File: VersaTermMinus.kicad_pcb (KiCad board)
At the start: 2 copper layers, 86.2 x 78 mm, 61 parts, among them CN1 HDMI_A, CN2 DE15_Socket, CN3 USB_B_Micro, CN5 USB-A, CN6 Mini-DIN-6, CN7 TTL Serial, CN8 DE9 Socket, J2 USBDATA, Q1 2N7002, Q2 2N7002, Q3 2N7002, Q4 2N7002, Q5 2N7002, Q6 2N7002, Q7 2N7002, SW1 RESET, SW2 DEFAULTS, SW3 3V3/5V, U1 Raspberry Pi Pico, U3 MAX3232

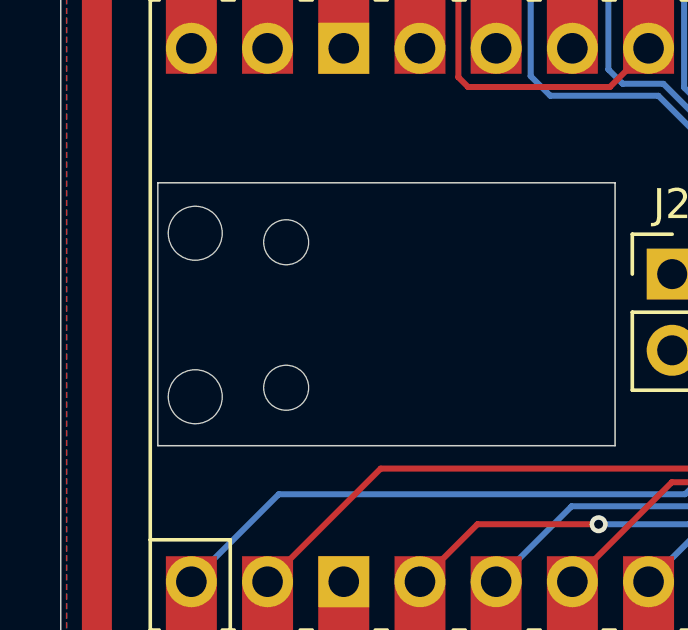
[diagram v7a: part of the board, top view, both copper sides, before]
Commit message: remove ambiguous drill holes
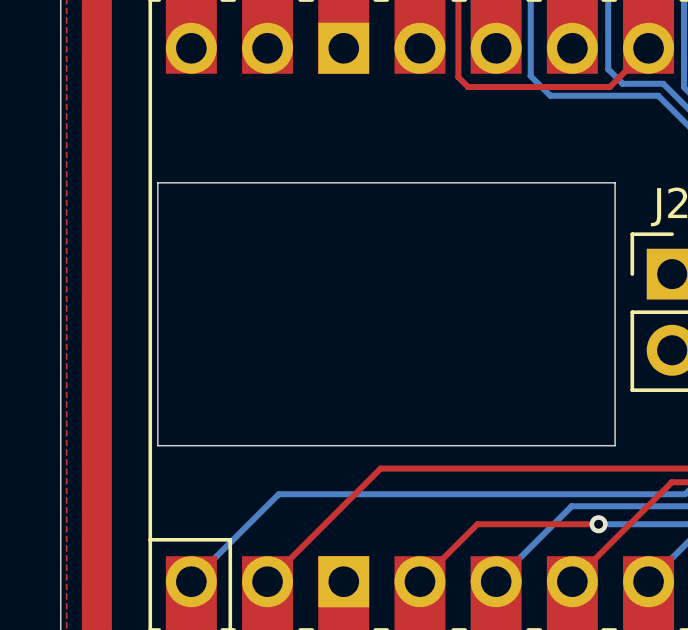
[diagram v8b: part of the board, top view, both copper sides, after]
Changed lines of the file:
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@@
 	(net 81 "RESET")
 	(net 82 "DEFAULTS")
-	(net 83 "unconnected-(U1-GND-Pad42)")
-	(net 84 "unconnected-(U1-3v3_EN-Pad37)")
-	(net 85 "unconnected-(CN6-Pad1)")
-	(net 86 "unconnected-(U1-SWDIO-Pad43)")
-	(net 87 "unconnected-(U1-SWCLK-Pad41)")
-	(net 88 "unconnected-(U1-ADC_VREF-Pad35)")
-	(net 89 "unconnected-(CN6-Pad5)")
-	(net 90 "unconnected-(U1-3v3_EN-Pad37)_1")
-	(net 91 "unconnected-(U1-ADC_VREF-Pad35)_1")
-	(net 92 "unconnected-(U1-VBUS-Pad40)")
-	(net 93 "unconnected-(U1-SWDIO-Pad43)_1")
-	(net 94 "unconnected-(U1-SWCLK-Pad41)_1")
-	(net 95 "unconnected-(U1-VBUS-Pad40)_1")
-	(net 96 "unconnected-(U1-GND-Pad42)_1")
-	(net 97 "/Sync")
-	(net 98 "/Red")
-	(net 99 "/Green")
-	(net 100 "/Blue")
+	(net 83 "unconnected-(CN6-Pad1)")
+	(net 84 "unconnected-(U1-ADC_VREF-Pad35)")
+	(net 85 "unconnected-(CN6-Pad5)")
+	(net 86 "unconnected-(U1-3v3_EN-Pad37)_1")
+	(net 87 "unconnected-(U1-VBUS-Pad40)")
+	(net 88 "unconnected-(U1-SWDIO-Pad43)_1")
+	(net 89 "unconnected-(U1-SWCLK-Pad41)_1")
+	(net 90 "unconnected-(U1-GND-Pad42)_1")
+	(net 91 "/Sync")
+	(net 92 "/Red")
+	(net 93 "/Green")
+	(net 94 "/Blue")
 	(footprint "Resistor_SMD:R_0805_2012Metric_Pad1.20x1.40mm_HandSolder"
 		(layer "F.Cu")
@@
 			(layers "F.Cu" "F.Paste" "F.Mask")
 			(roundrect_rratio 0.208333)
-			(net 98 "/Red")
+			(net 92 "/Red")
 			(pintype "passive")
 		)
@@
 			(layers "*.Cu" "*.Mask")
 			(remove_unused_layers no)
-			(net 85 "unconnected-(CN6-Pad1)")
+			(net 83 "unconnected-(CN6-Pad1)")
 			(pintype "passive+no_connect")
 		)
@@
 			(layers "*.Cu" "*.Mask")
 			(remove_unused_layers no)
-			(net 89 "unconnected-(CN6-Pad5)")
+			(net 85 "unconnected-(CN6-Pad5)")
 			(pintype "passive+no_connect")
 		)
@@
 			(layers "F.Cu" "F.Paste" "F.Mask")
 			(roundrect_rratio 0.208333)
-			(net 100 "/Blue")
+			(net 94 "/Blue")
 			(pintype "passive")
 		)
@@
 			(layer "F.SilkS")
 		)
-		(fp_poly
-			(pts
-				(xy 3.7 -20.2) (xy -3.7 -20.2) (xy -3.7 -24.9) (xy 3.7 -24.9)
-			)
-			(stroke
-				(width 0.1)
-				(type solid)
-			)
-			(fill solid)
-			(layer "Dwgs.User")
-		)
-		(fp_poly
-			(pts
-				(xy -1.5 -16.5) (xy -3.5 -16.5) (xy -3.5 -18.5) (xy -1.5 -18.5)
-			)
-			(stroke
-				(width 0.1)
-				(type solid)
-			)
-			(fill solid)
-			(layer "Dwgs.User")
-		)
-		(fp_poly
-			(pts
-				(xy -1.5 -14) (xy -3.5 -14) (xy -3.5 -16) (xy -1.5 -16)
-			)
-			(stroke
-				(width 0.1)
-				(type solid)
-			)
-			(fill solid)
-			(layer "Dwgs.User")
-		)
-		(fp_poly
-			(pts
-				(xy -1.5 -11.5) (xy -3.5 -11.5) (xy -3.5 -13.5) (xy -1.5 -13.5)
-			)
-			(stroke
-				(width 0.1)
-				(type solid)
-			)
-			(fill solid)
-			(layer "Dwgs.User")
-		)
 		(fp_line
 			(start 11 -26)
@@
 			)
 		)
-		(pad "" np_thru_hole oval
-			(at -2.725 -24 90)
-			(size 1.8 1.8)
-			(drill 1.8)
-			(layers "*.Cu" "*.Mask")
-		)
-		(pad "" np_thru_hole oval
-			(at -2.425 -20.97 90)
-			(size 1.5 1.5)
-			(drill 1.5)
-			(layers "*.Cu" "*.Mask")
-		)
-		(pad "" np_thru_hole oval
-			(at 2.425 -20.97 90)
-			(size 1.5 1.5)
-			(drill 1.5)
-			(layers "*.Cu" "*.Mask")
-		)
-		(pad "" np_thru_hole oval
-			(at 2.725 -24 90)
-			(size 1.8 1.8)
-			(drill 1.8)
-			(layers "*.Cu" "*.Mask")
-		)
 		(pad "1" thru_hole oval
 			(at -8.89 -24.13 90)
@@
 			(layers "*.Cu" "*.Mask")
 			(remove_unused_layers no)
-			(net 88 "unconnected-(U1-ADC_VREF-Pad35)")
+			(net 84 "unconnected-(U1-ADC_VREF-Pad35)")
 			(pinfunction "ADC_VREF")
 			(pintype "input+no_connect")
@@
 			)
 			(layers "F.Cu" "F.Mask")
-			(net 91 "unconnected-(U1-ADC_VREF-Pad35)_1")
+			(net 84 "unconnected-(U1-ADC_VREF-Pad35)")
 			(pinfunction "ADC_VREF")
 			(pintype "input+no_connect")
@@
 			(layers "*.Cu" "*.Mask")
 			(remove_unused_layers no)
-			(net 90 "unconnected-(U1-3v3_EN-Pad37)_1")
+			(net 86 "unconnected-(U1-3v3_EN-Pad37)_1")
 			(pinfunction "3v3_EN")
 			(pintype "input+no_connect")
@@
 			)
 			(layers "F.Cu" "F.Mask")
-			(net 84 "unconnected-(U1-3v3_EN-Pad37)")
+			(net 86 "unconnected-(U1-3v3_EN-Pad37)_1")
 			(pinfunction "3v3_EN")
 			(pintype "input+no_connect")
@@
 			(layers "*.Cu" "*.Mask")
 			(remove_unused_layers no)
-			(net 92 "unconnected-(U1-VBUS-Pad40)")
+			(net 87 "unconnected-(U1-VBUS-Pad40)")
 			(pinfunction "VBUS")
 			(pintype "power_in+no_connect")
@@
 			)
 			(layers "F.Cu" "F.Mask")
-			(net 95 "unconnected-(U1-VBUS-Pad40)_1")
+			(net 87 "unconnected-(U1-VBUS-Pad40)")
 			(pinfunction "VBUS")
 			(pintype "power_in+no_connect")
@@
 			(layers "*.Cu" "*.Mask")
 			(remove_unused_layers no)
-			(net 94 "unconnected-(U1-SWCLK-Pad41)_1")
+			(net 89 "unconnected-(U1-SWCLK-Pad41)_1")
 			(pinfunction "SWCLK")
 			(pintype "bidirectional+no_connect")
@@
 			)
 			(layers "F.Cu" "F.Mask")
-			(net 87 "unconnected-(U1-SWCLK-Pad41)")
+			(net 89 "unconnected-(U1-SWCLK-Pad41)_1")
 			(pinfunction "SWCLK")
 			(pintype "bidirectional+no_connect")
@@
 			(layers "*.Cu" "*.Mask")
 			(remove_unused_layers no)
-			(net 96 "unconnected-(U1-GND-Pad42)_1")
+			(net 90 "unconnected-(U1-GND-Pad42)_1")
 			(pinfunction "GND")
 			(pintype "passive+no_connect")
@@
 			)
 			(layers "F.Cu" "F.Mask")
-			(net 83 "unconnected-(U1-GND-Pad42)")
+			(net 90 "unconnected-(U1-GND-Pad42)_1")
 			(pinfunction "GND")
 			(pintype "passive+no_connect")
@@
 			(layers "*.Cu" "*.Mask")
 			(remove_unused_layers no)
-			(net 93 "unconnected-(U1-SWDIO-Pad43)_1")
+			(net 88 "unconnected-(U1-SWDIO-Pad43)_1")
 			(pinfunction "SWDIO")
 			(pintype "bidirectional+no_connect")
@@
 			)
 			(layers "F.Cu" "F.Mask")
-			(net 86 "unconnected-(U1-SWDIO-Pad43)")
+			(net 88 "unconnected-(U1-SWDIO-Pad43)_1")
 			(pinfunction "SWDIO")
 			(pintype "bidirectional+no_connect")
@@
 			(layers "F.Cu" "F.Paste" "F.Mask")
 			(roundrect_rratio 0.208333)
-			(net 99 "/Green")
+			(net 93 "/Green")
 			(pintype "passive")
 		)
@@
 			(layers "*.Cu" "*.Mask")
 			(remove_unused_layers no)
-			(net 98 "/Red")
+			(net 92 "/Red")
 			(pintype "passive")
 		)
@@
 			(layers "*.Cu" "*.Mask")
 			(remove_unused_layers no)
-			(net 99 "/Green")
+			(net 93 "/Green")
 			(pintype "passive")
 		)
@@
 			(layers "*.Cu" "*.Mask")
 			(remove_unused_layers no)
-			(net 100 "/Blue")
+			(net 94 "/Blue")
 			(pintype "passive")
 		)
@@
 			(layers "*.Cu" "*.Mask")
 			(remove_unused_layers no)
-			(net 97 "/Sync")
+			(net 91 "/Sync")
 			(pintype "passive")
 		)
@@
 			(layers "F.Cu" "F.Paste" "F.Mask")
 			(roundrect_rratio 0.208333)
-			(net 97 "/Sync")
+			(net 91 "/Sync")
 			(pintype "passive")
 		)
@@
 			(layers "F.Cu" "F.Paste" "F.Mask")
 			(roundrect_rratio 0.208333)
-			(net 99 "/Green")
+			(net 93 "/Green")
 			(pintype "passive")
 		)
@@
 			(layers "F.Cu" "F.Paste" "F.Mask")
 			(roundrect_rratio 0.208333)
-			(net 99 "/Green")
+			(net 93 "/Green")
 			(pintype "passive")
 		)
@@
 			(layers "F.Cu" "F.Paste" "F.Mask")
 			(roundrect_rratio 0.208333)
-			(net 98 "/Red")
+			(net 92 "/Red")
 			(pintype "passive")
 		)
@@
 			(layers "F.Cu" "F.Paste" "F.Mask")
 			(roundrect_rratio 0.208333)
-			(net 100 "/Blue")
+			(net 94 "/Blue")
 			(pintype "passive")
 		)
@@
 			(layers "F.Cu" "F.Paste" "F.Mask")
 			(roundrect_rratio 0.208333)
-			(net 98 "/Red")
+			(net 92 "/Red")
 			(pintype "passive")
 		)
@@
 		(width 0.2)
 		(layer "F.Cu")
-		(net 97)
+		(net 91)
 	)
 	(segment
@@
 		(width 0.2)
 		(layer "F.Cu")
-		(net 97)
+		(net 91)
 	)
 	(segment
@@
 		(width 0.2)
 		(layer "F.Cu")
-		(net 97)
+		(net 91)
 	)
 	(segment
@@
 		(width 0.2)
 		(layer "F.Cu")
-		(net 97)
+		(net 91)
 	)
 	(segment
@@
 		(width 0.2)
 		(layer "F.Cu")
-		(net 98)
+		(net 92)
 	)
 	(segment
@@
 		(width 0.2)
 		(layer "F.Cu")
-		(net 98)
+		(net 92)
 	)
 	(segment
@@
 		(width 0.2)
 		(layer "F.Cu")
-		(net 98)
+		(net 92)
 	)
 	(segment
@@
 		(width 0.2)
 		(layer "F.Cu")
-		(net 99)
+		(net 93)
 	)
 	(segment
@@
 		(width 0.2)
 		(layer "F.Cu")
-		(net 99)
+		(net 93)
 	)
 	(segment
@@
 		(width 0.2)
 		(layer "F.Cu")
-		(net 99)
+		(net 93)
 	)
 	(segment
@@
 		(width 0.2)
 		(layer "F.Cu")
-		(net 100)
+		(net 94)
 	)
 	(segment
@@
 		(width 0.2)
 		(layer "F.Cu")
-		(net 100)
+		(net 94)
 	)
 	(segment
@@
 		(width 0.2)
 		(layer "F.Cu")
-		(net 100)
+		(net 94)
 	)
 	(segment
@@
 		(width 0.2)
 		(layer "F.Cu")
-		(net 100)
+		(net 94)
 	)
 	(segment
@@
 		(width 0.2)
 		(layer "F.Cu")
-		(net 100)
+		(net 94)
 	)
 	(segment
@@
 		(width 0.2)
 		(layer "F.Cu")
-		(net 100)
+		(net 94)
 	)
 	(segment
@@
 		(width 0.2)
 		(layer "F.Cu")
-		(net 100)
+		(net 94)
 	)
 	(zone
